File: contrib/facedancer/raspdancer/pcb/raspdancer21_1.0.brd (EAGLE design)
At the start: 25.8 x 33.3 mm, 15 parts, among them Q1 12Mhz

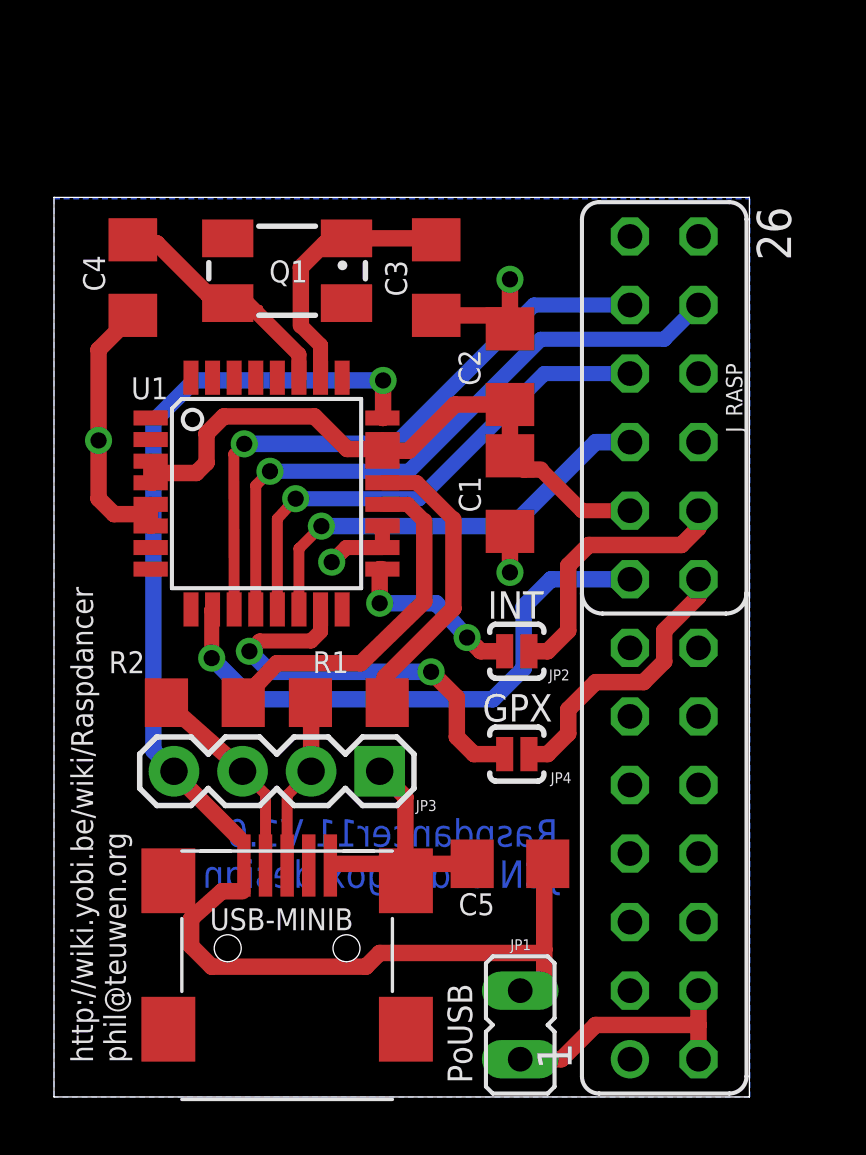
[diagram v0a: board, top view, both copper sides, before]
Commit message: Add raspdancer21 sch & brd
git-svn-id: https://svn.code.sf.net/p/goodfet/code@1588 12e2690d-a6be-4b82-a7b7-67c4a43b65c8
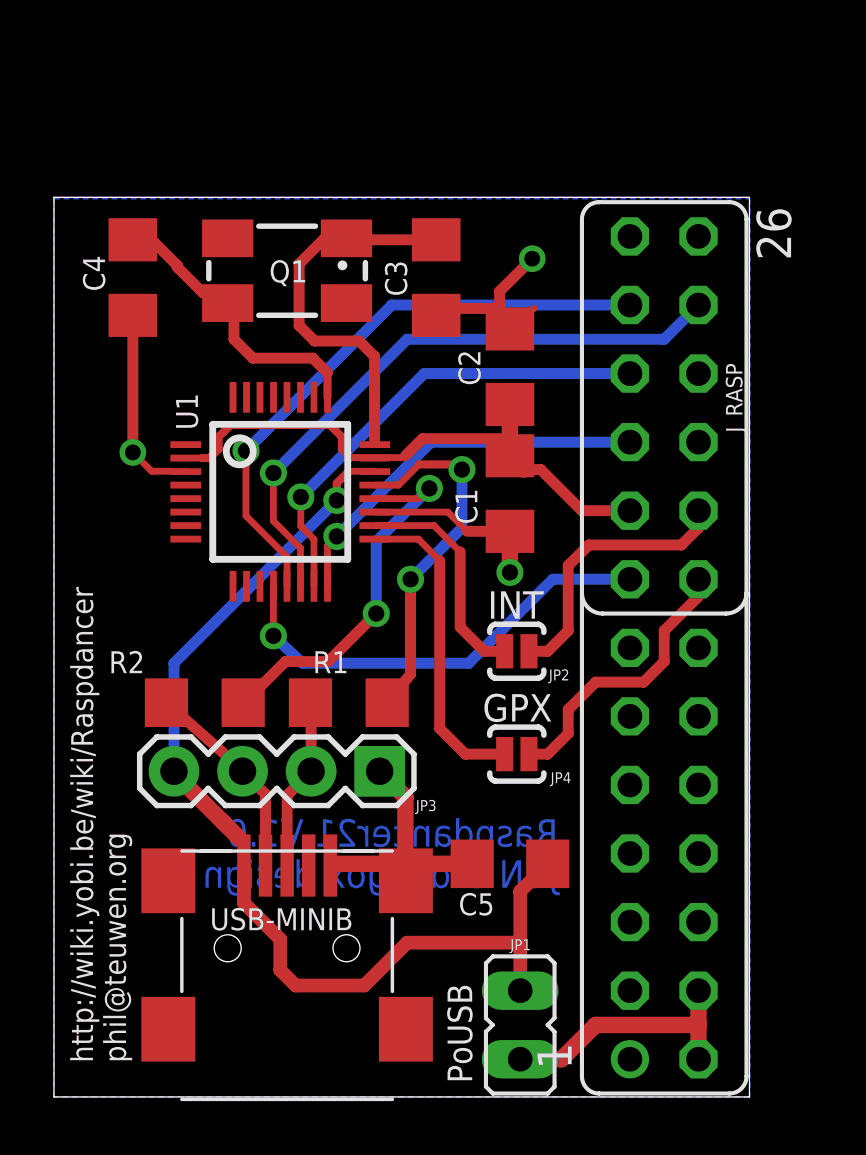
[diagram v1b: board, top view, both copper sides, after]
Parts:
- U1: value (none) -> MAX3421E; device maxim-2:TQFP32-08 -> SparkFun-DigitalIC:TQFP32-5MM
- moved U1 0.51 mm to (8.38, 22.4)
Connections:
- removed net SLCK: J_RASP.23, U1.11
- removed net VBUS: C5.2, JP1.1, JP3.4, U1.24, USB-MINIB.VBUS
- new net SCLK: J_RASP.23, U1.13
- new net VBCOMP: C5.2, JP1.1, JP3.4, U1.22, USB-MINIB.VBUS
- net GND: now also U1.3; no longer U1.18, U1.5, U1.6
- net GPX: now also U1.17; no longer U1.15
- net INT: now also U1.18; no longer U1.17
- net IX: now also C4.1, Q1.3, U1.25; no longer C3.1, Q1.1, U1.26
- net MISO: now also U1.15; no longer U1.13
- net MOSI: now also U1.16; no longer U1.14
- net RES: now also U1.12; no longer U1.10
- net SS: now also U1.14; no longer U1.12
- net VCC: now also U1.2; no longer U1.22, U1.3, U1.4
- net XO: now also C3.1, Q1.1, U1.24; no longer C4.1, Q1.3, U1.27
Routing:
- net VBUS: track 50.0 -> 0.00 mm, vias 1 -> 0
- net VBCOMP: track 0.00 -> 38.2 mm, vias 0 -> 1
- net SLCK: track 22.7 -> 0.00 mm, vias 1 -> 0
- net SCLK: track 0.00 -> 22.1 mm, vias 0 -> 1
- net RES: track 21.1 -> 16.7 mm
- net XO: track 10.7 -> 14.9 mm
- net GPX: track 15.6 -> 11.8 mm, vias 2 -> 0
- net VCC: track 25.3 -> 22.0 mm
- net D+: track 11.1 -> 13.4 mm, vias 0 -> 2
- net MOSI: track 16.1 -> 14.3 mm
- net INT: track 6.77 -> 8.38 mm, vias 2 -> 0
- net GND: track 29.7 -> 31.3 mm, vias 4 -> 3
- net IX: track 10.4 -> 11.6 mm
- net MISO: track 18.7 -> 17.6 mm
- net SS: track 23.8 -> 22.9 mm
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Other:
- board text added: "Raspdancer21 V1.0 JCN & doegox design"
- board text removed: "Raspdancer11 V1.0 JCN & doegox design"

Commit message: raspdancer pcb edited
thanks to Zac Franken for his tuning tips

git-svn-id: https://svn.code.sf.net/p/goodfet/code@1589 12e2690d-a6be-4b82-a7b7-67c4a43b65c8
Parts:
- removed C5: 1uF, 00_mylib:C1206
- removed JP3: (no value), SparkFun:1X04
- added JP5: USB-A-S, SparkFun-Connectors:USB-A-S
- J_RASP: device con-lsta:FE13-2 -> doegox:FE13-2
- moved C1 14.3 mm to (18.2, 8.13), turned to 270 degrees
- moved Q1 6.92 mm to (15.4, 29.0)
- moved C3 5.27 mm to (8.89, 30.5), turned to 180 degrees
- moved C2 3.63 mm to (16.6, 23.4), turned to 90 degrees
- moved R1 1.20 mm to (11.3, 13.5)
- moved R2 1.20 mm to (5.97, 13.5)
- moved C4 1.08 mm to (3.62, 29.5), turned to 180 degrees
- moved JP2 0.38 mm to (16.8, 16.5)
- moved JP4 0.38 mm to (16.8, 12.7)
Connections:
- removed net VBCOMP: C5.2, JP1.1, JP3.4, U1.22, USB-MINIB.VBUS
- new net VBUS: C1.2, JP1.1, JP5.VBUS, U1.22, USB-MINIB.VBUS
- net D+2: now also JP5.D+; no longer JP3.2
- net D-2: now also JP5.D-; no longer JP3.3
- net GND: now also JP5.GND; no longer C5.1, JP3.1
- net VCC: no longer C1.2
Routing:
- net VBUS: track 0.00 -> 46.4 mm, vias 0 -> 1
- net VBCOMP: track 38.2 -> 0.00 mm, vias 1 -> 0
- net GND: track 31.3 -> 58.8 mm, vias 3 -> 4
- net D-2: track 7.70 -> 14.9 mm, vias 0 -> 1
- net XO: track 14.9 -> 17.7 mm
- net D+2: track 6.35 -> 8.99 mm, vias 0 -> 1
- net D-: track 14.2 -> 15.9 mm
- net VCC: track 22.0 -> 20.8 mm, vias 0 -> 1
- net D+: track 13.4 -> 14.6 mm
- net IX: track 11.6 -> 10.6 mm
- net SCLK: track 22.1 -> 22.9 mm
- net GPX2: track 10.5 -> 11.2 mm, vias 0 -> 1
- net INT2: track 10.2 -> 10.8 mm, vias 0 -> 1
- net SS: track 22.9 -> 23.5 mm
- net VBUS2: track 10.2 -> 9.67 mm
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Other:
- board text added: "Raspdancer21 V1.0 by JCN & doegox"
- board text removed: "Raspdancer21 V1.0 JCN & doegox design"

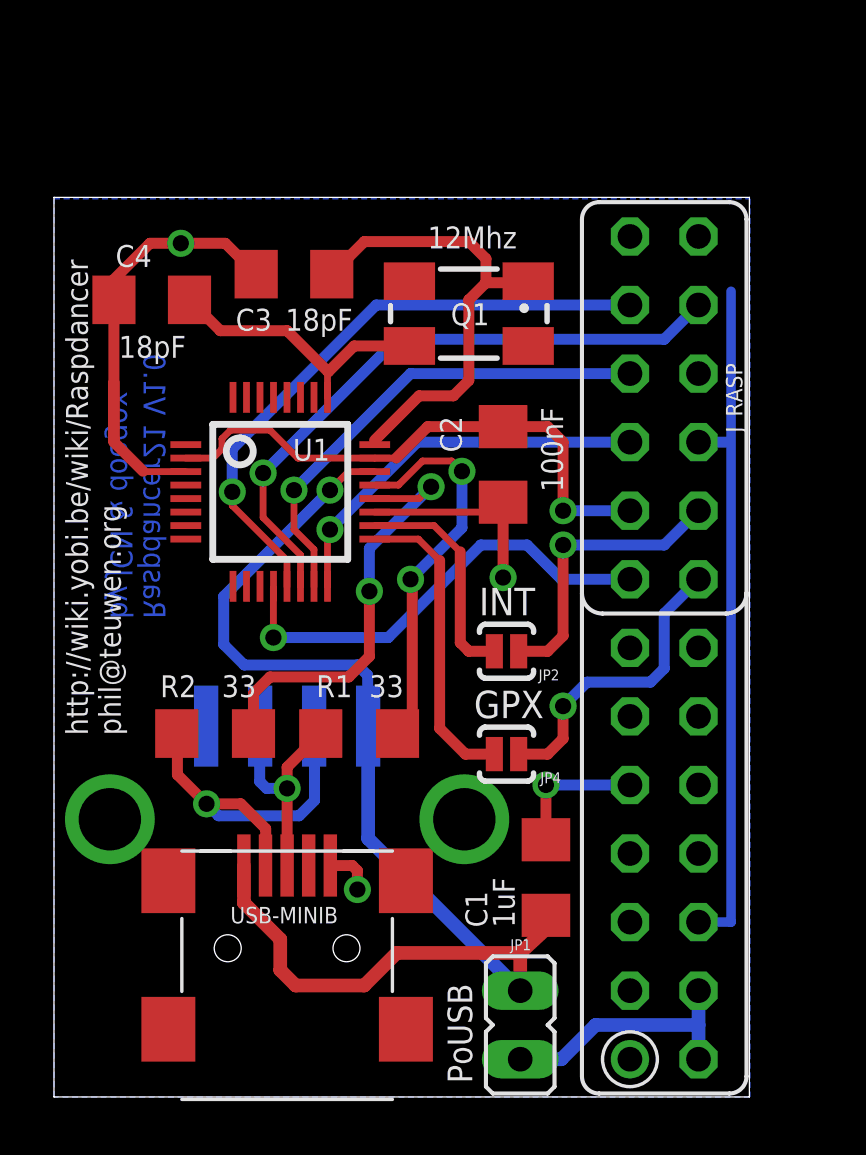
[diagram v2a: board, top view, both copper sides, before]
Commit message: raspdancer21: fix silkscreen
git-svn-id: https://svn.code.sf.net/p/goodfet/code@1590 12e2690d-a6be-4b82-a7b7-67c4a43b65c8
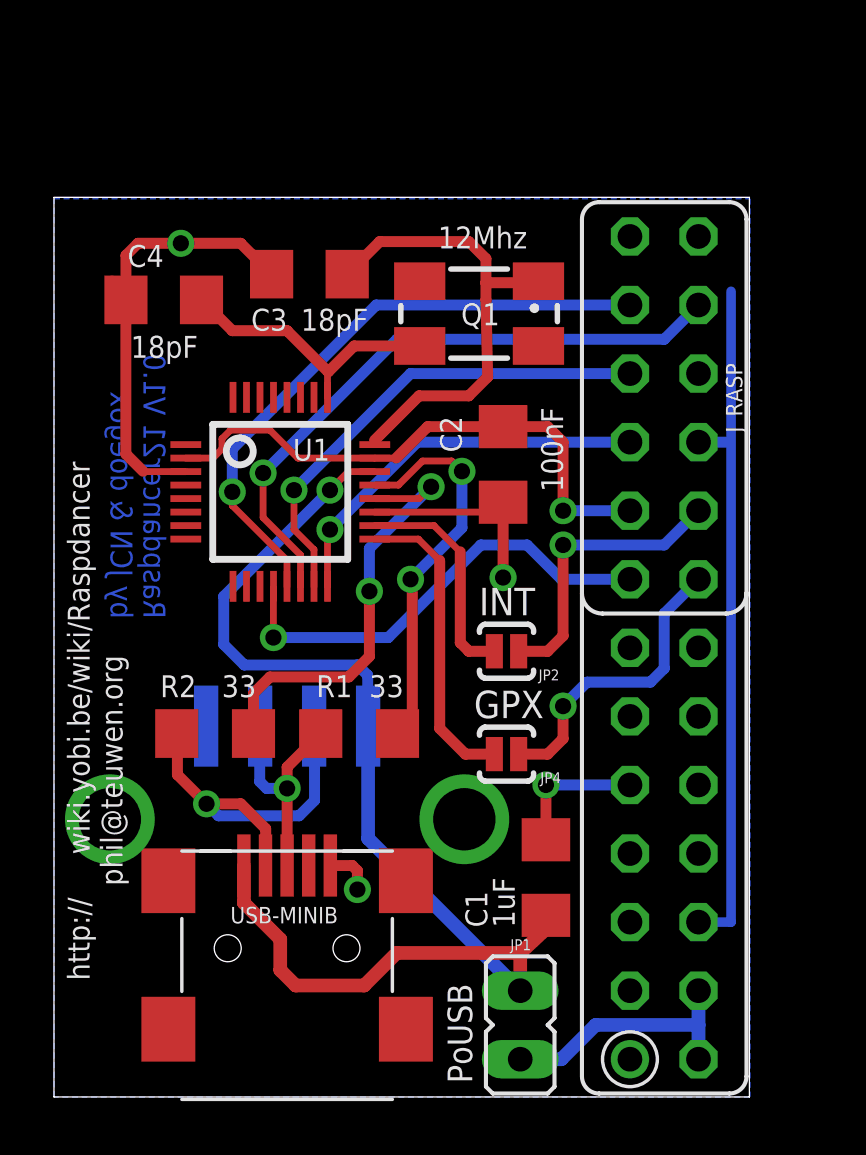
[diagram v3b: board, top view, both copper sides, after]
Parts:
- moved C3 0.57 mm to (9.46, 30.5)
- moved C4 0.44 mm to (4.06, 29.5)
- moved Q1 0.38 mm to (15.7, 29.0)
- renumbered JP5 to USB-A
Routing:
- net GND: track 58.8 -> 58.2 mm
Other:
- board text added: "http:// wiki.yobi.be/wiki/Raspdancer phil@teuwen.org"
- board text removed: "http://wiki.yobi.be/wiki/Raspdancer phil@teuwen.org"

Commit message: raspdancer11/21 PCB: more room along connector & larger vias for raspdancer11
git-svn-id: https://svn.code.sf.net/p/goodfet/code@1591 12e2690d-a6be-4b82-a7b7-67c4a43b65c8
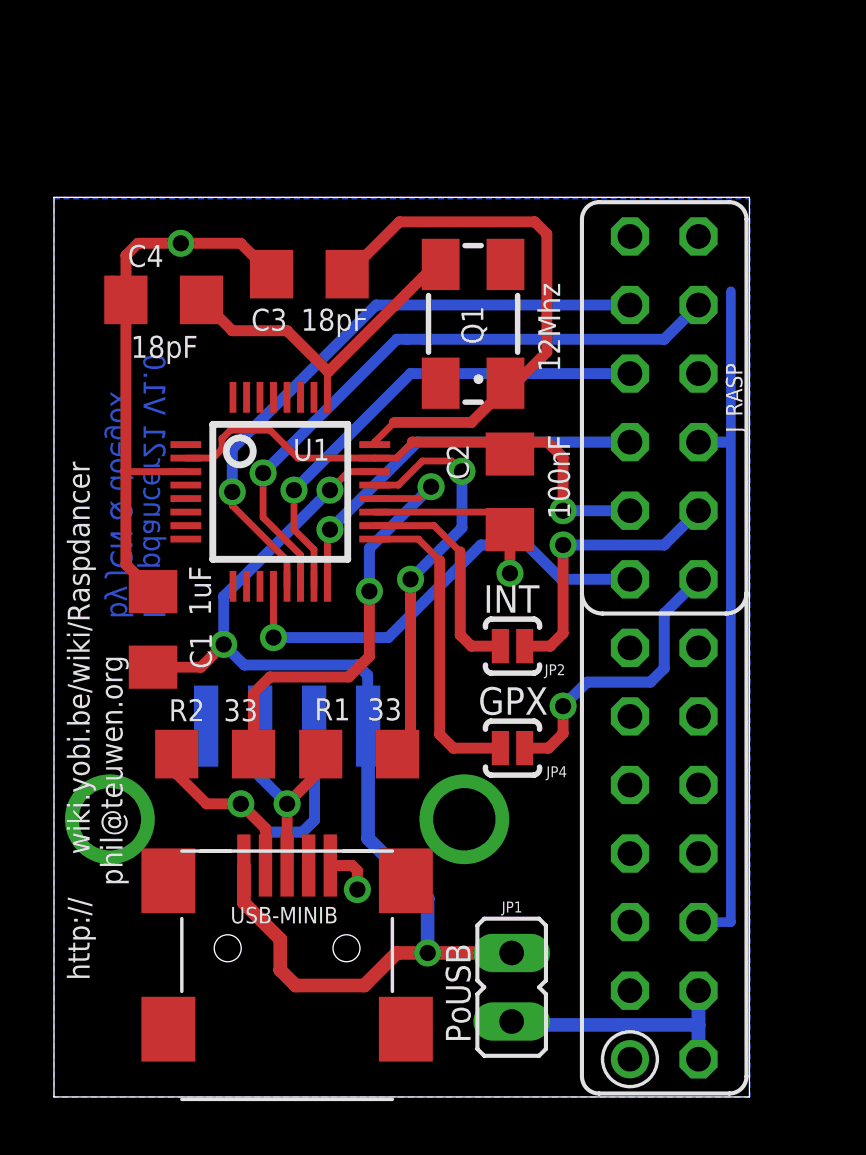
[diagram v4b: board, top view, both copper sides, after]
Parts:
- moved C1 17.2 mm to (3.67, 17.3)
- moved JP1 1.43 mm to (17.0, 4.06)
- moved C2 1.05 mm to (16.9, 22.4)
- moved R1 0.76 mm to (11.3, 12.7)
- moved R2 0.76 mm to (5.97, 12.7)
- moved Q1 0.44 mm to (15.5, 28.6), turned to 90 degrees
- moved JP4 0.31 mm to (17.0, 12.9)
- moved JP2 0.29 mm to (17.0, 16.7)
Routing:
- net GND: track 58.2 -> 62.5 mm, vias 4 -> 3
- net VBUS: track 46.4 -> 43.0 mm, vias 1 -> 3
- net XO: track 18.0 -> 20.7 mm
- net IX: track 10.5 -> 12.6 mm
- net D-2: track 14.9 -> 13.1 mm
- net D+: track 14.6 -> 15.5 mm
- net D-: track 15.9 -> 16.6 mm
- net D+2: track 8.99 -> 8.36 mm

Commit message: raspdancer: larger wires & vias & some tunings
git-svn-id: https://svn.code.sf.net/p/goodfet/code@1592 12e2690d-a6be-4b82-a7b7-67c4a43b65c8
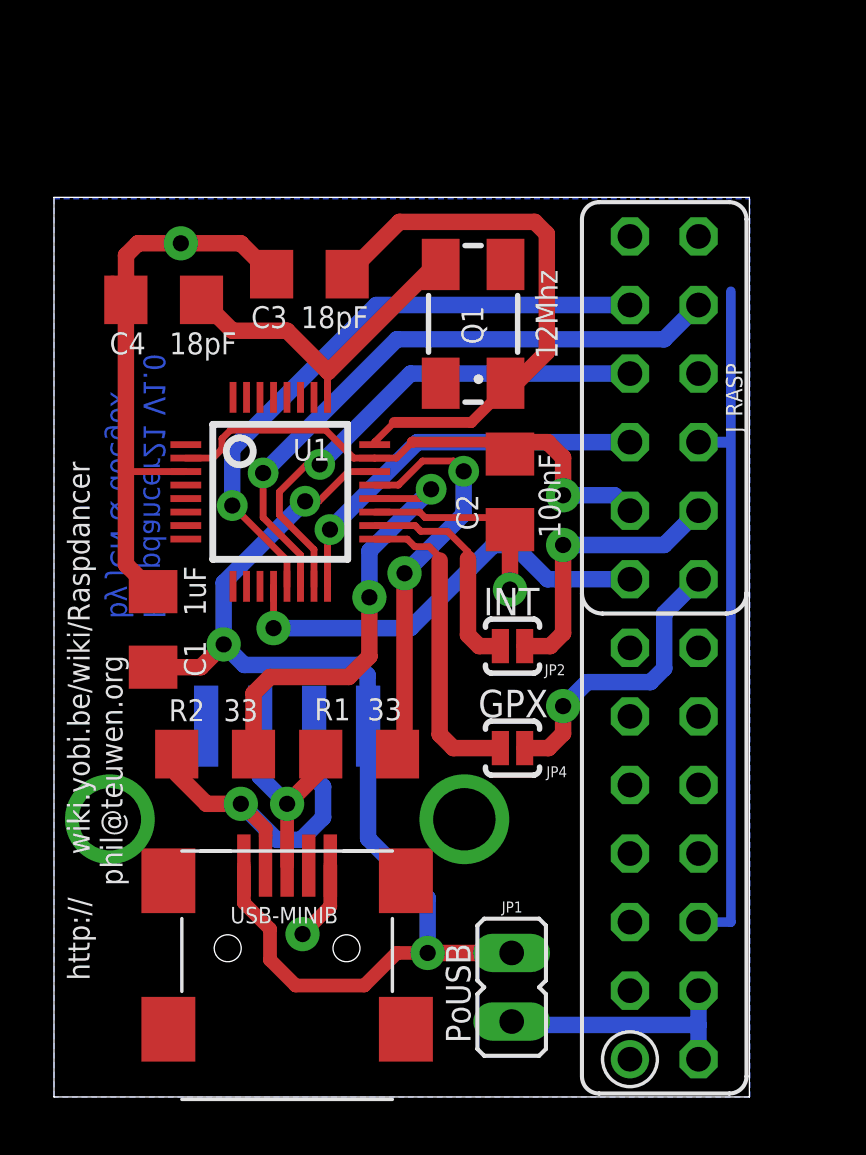
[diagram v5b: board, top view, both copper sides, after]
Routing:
- net GND: track 62.5 -> 64.6 mm
- net MISO: track 18.1 -> 18.8 mm
- net D-2: track 13.1 -> 13.8 mm
